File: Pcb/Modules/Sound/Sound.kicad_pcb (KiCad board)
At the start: 2 copper layers, 50.8 x 20.3 mm, 18 parts, among them J1 JACK_RJ45, U1 MAX4466, X1 HOLE, X2 HOLE, X3 HOLE, X4 HOLE

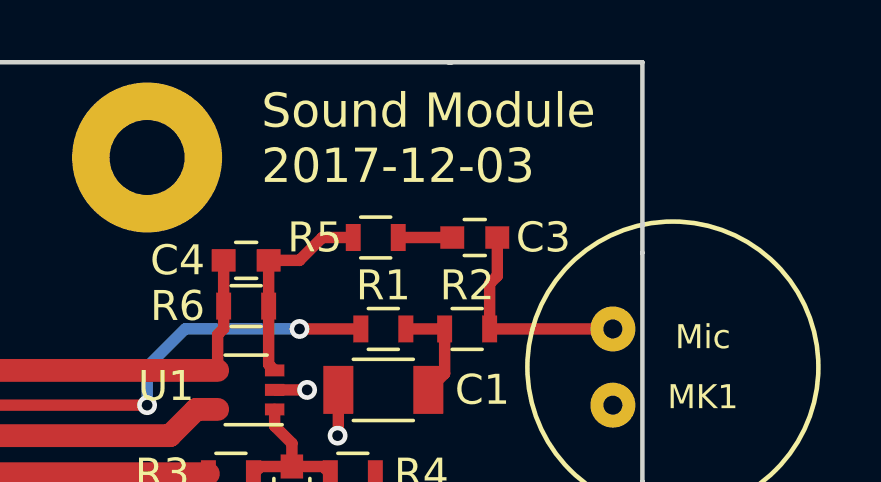
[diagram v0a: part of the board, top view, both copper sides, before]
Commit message: Update CA6 PCB.  Also update versions of all the module pcbs to match.
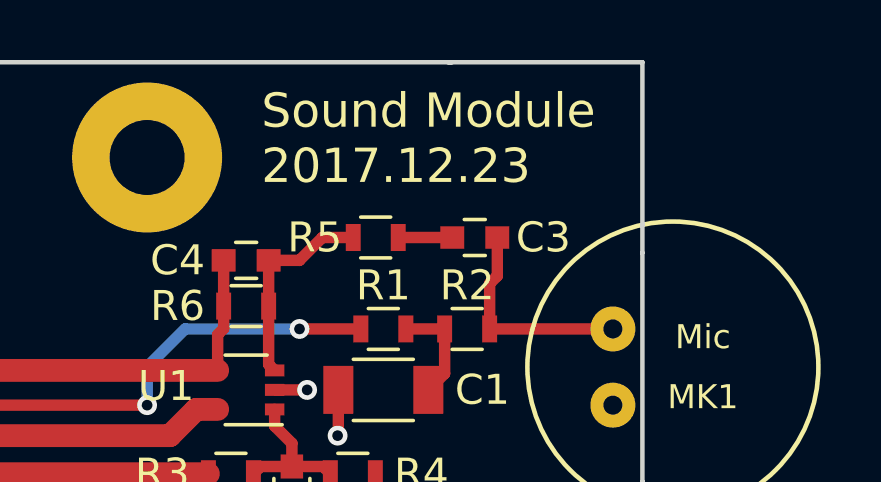
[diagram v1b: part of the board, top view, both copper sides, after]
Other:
- board text added: "Sound Module 2017.12.23"
- board text removed: "Sound Module 2017-12-03"
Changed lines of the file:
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@@
     (links 26)
     (no_connects 0)
-    (area 25.324999 25.324999 76.275001 45.795001)
+    (area 22.381869 24.0968 82.345401 47.1232)
     (thickness 1.6)
     (drawings 13)
@@
   (gr_line (start 69.85 45.72) (end 31.75 45.72) (angle 90) (layer Edge.Cuts) (width 0.15))
   (gr_line (start 31.75 25.4) (end 69.85 25.4) (angle 90) (layer Edge.Cuts) (width 0.15))
-  (gr_text "Sound Module\n2017-12-03" (at 63.5 27.94) (layer F.SilkS)
+  (gr_text "Sound Module\n2017.12.23" (at 63.5 27.94) (layer F.SilkS)
     (effects (font (size 1.143 1.143) (thickness 0.2286)) (justify left))
   )

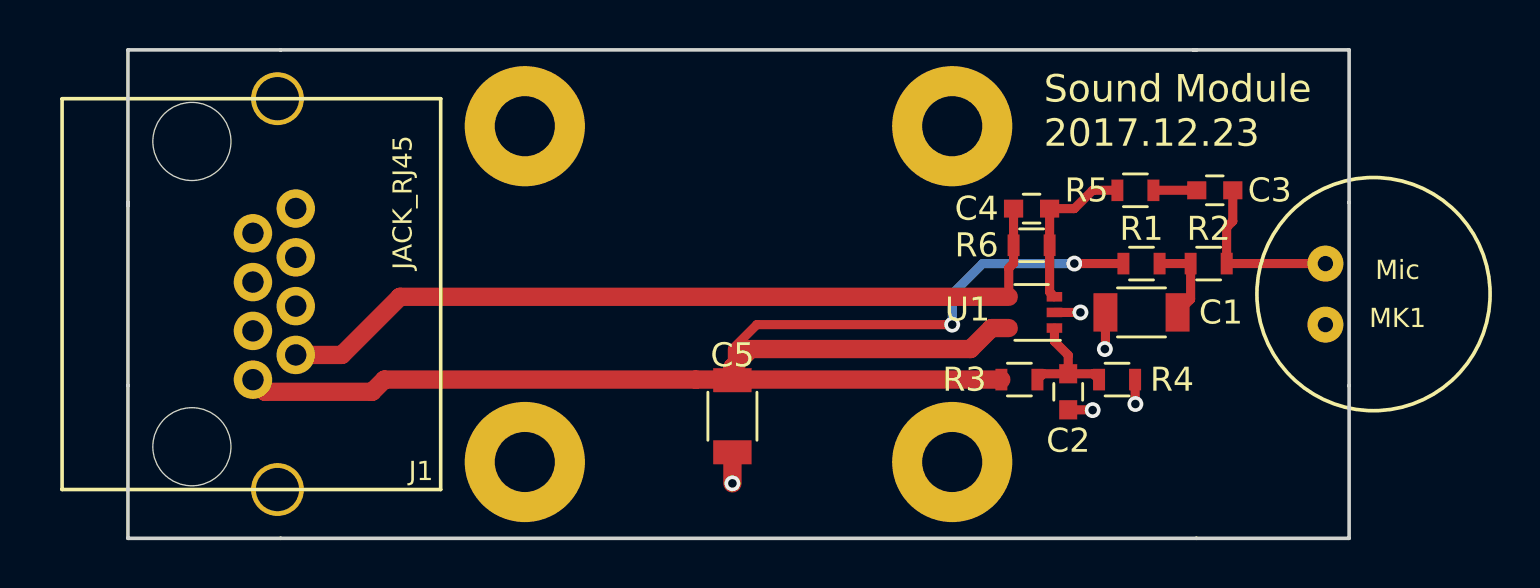
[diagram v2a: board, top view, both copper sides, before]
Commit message: Update module pcbs
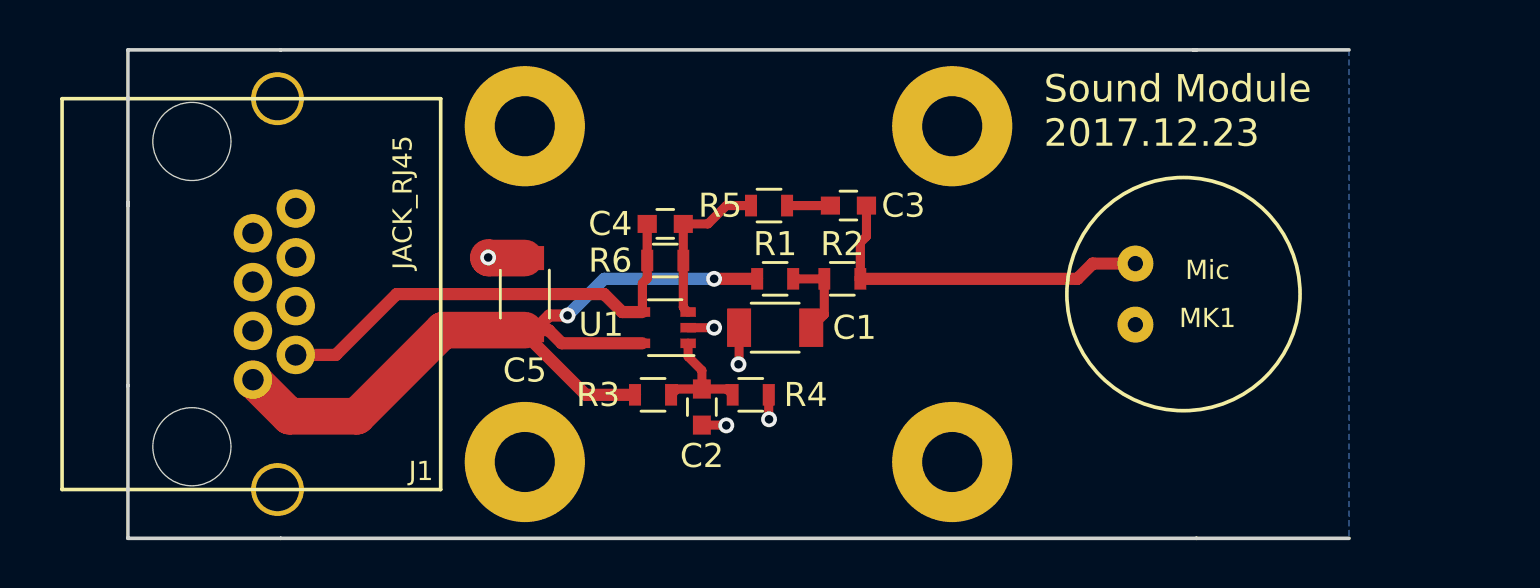
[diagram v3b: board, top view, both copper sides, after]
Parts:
- moved C2 15.3 mm to (49.3, 40.3)
- moved R2 15.3 mm to (55.1, 34.9)
- moved R3 15.3 mm to (47.2, 39.8)
- moved R4 15.3 mm to (51.3, 39.8)
- moved R5 15.3 mm to (52.1, 31.9)
- moved C1 15.3 mm to (52.3, 37.0)
- moved C3 15.3 mm to (55.4, 31.9)
- moved C4 15.3 mm to (47.8, 32.6)
- moved R1 15.3 mm to (52.3, 34.9)
- moved R6 15.3 mm to (47.8, 34.2)
- moved U1 15.3 mm to (47.8, 37.0)
- moved C5 10.0 mm to (41.9, 35.6), turned to 270 degrees
- moved MK1 7.91 mm to (69.3, 35.6)
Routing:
- net +3V3: track 65.6 -> 34.9 mm
- net /AN_VAL: track 34.4 -> 19.5 mm
- net Net-(C3-Pad1): track 7.01 -> 14.9 mm
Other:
- outline, holes or cut-outs redrawn

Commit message: Move holes on sound module to match other modules.  Updated silkscreens on other modules.  Generate gerbers
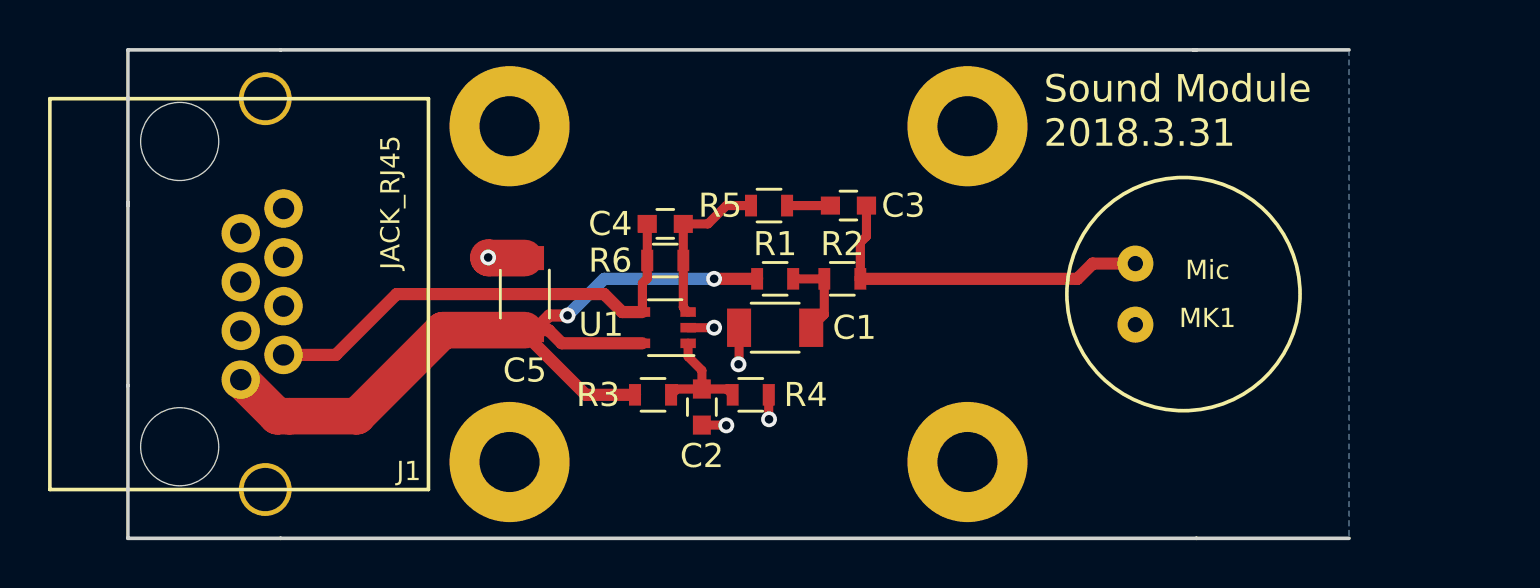
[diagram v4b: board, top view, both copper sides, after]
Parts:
- moved X3 0.64 mm to (60.3, 28.6)
- moved X4 0.64 mm to (60.3, 42.5)
- moved X1 0.63 mm to (41.3, 28.6)
- moved X2 0.63 mm to (41.3, 42.5)
- moved J1 0.51 mm to (30.0, 35.6)
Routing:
- net /AN_VAL: track 19.5 -> 20.0 mm
- net +3V3: track 34.9 -> 35.4 mm
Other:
- board text added: "Sound Module 2018.3.31"
- board text removed: "Sound Module 2017.12.23"
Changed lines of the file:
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@@
     (thickness 1.6)
     (drawings 11)
-    (tracks 65)
+    (tracks 66)
     (zones 0)
     (modules 18)
@@
   )
   (setup
-    (last_trace_width 0.254)
+    (last_trace_width 1.524)
     (user_trace_width 0.381)
     (user_trace_width 0.508)
@@
   )
   (module CA6:RJ45_pcbwing (layer F.Cu)
-    (at 30.48 35.56 270)
+    (at 29.972 35.56 270)
     (fp_text reference J1 (at 7.366 -7.112 360) (layer F.SilkS)
       (effects (font (size 0.8 0.8) (thickness 0.15)))
@@
   )
   (module Mounting_Holes:MountingHole_2.5mm_Pad (layer F.Cu)
-    (at 41.91 28.575)
+    (at 41.275 28.575)
     (descr "Mounting Hole 2.5mm")
     (tags "mounting hole 2.5mm")
@@
       (effects (font (size 1 1) (thickness 0.15)))
     )
-    (fp_text user %R (at 0.3 0) (layer F.Fab)
+    (fp_text user %R (at 0.3 0) (layer F.Fab) hide
       (effects (font (size 1 1) (thickness 0.15)))
     )
@@
   )
   (module Mounting_Holes:MountingHole_2.5mm_Pad (layer F.Cu)
-    (at 41.91 42.545)
+    (at 41.275 42.545)
     (descr "Mounting Hole 2.5mm")
     (tags "mounting hole 2.5mm")
@@
       (effects (font (size 1 1) (thickness 0.15)))
     )
-    (fp_text user %R (at 0.3 0) (layer F.Fab)
+    (fp_text user %R (at 0.3 0) (layer F.Fab) hide
       (effects (font (size 1 1) (thickness 0.15)))
     )
@@
   )
   (module Mounting_Holes:MountingHole_2.5mm_Pad (layer F.Cu)
-    (at 59.69 28.575)
+    (at 60.325 28.575)
     (descr "Mounting Hole 2.5mm")
     (tags "mounting hole 2.5mm")
@@
       (effects (font (size 1 1) (thickness 0.15)))
     )
-    (fp_text user %R (at 0.3 0) (layer F.Fab)
+    (fp_text user %R (at 0.3 0) (layer F.Fab) hide
       (effects (font (size 1 1) (thickness 0.15)))
     )
@@
   )
   (module Mounting_Holes:MountingHole_2.5mm_Pad (layer F.Cu)
-    (at 59.69 42.545)
+    (at 60.325 42.545)
     (descr "Mounting Hole 2.5mm")
     (tags "mounting hole 2.5mm")
@@
       (effects (font (size 1 1) (thickness 0.15)))
     )
-    (fp_text user %R (at 0.3 0) (layer F.Fab)
+    (fp_text user %R (at 0.3 0) (layer F.Fab) hide
       (effects (font (size 1 1) (thickness 0.15)))
     )
@@
   (gr_line (start 69.85 45.72) (end 31.75 45.72) (angle 90) (layer Edge.Cuts) (width 0.15))
   (gr_line (start 31.75 25.4) (end 69.85 25.4) (angle 90) (layer Edge.Cuts) (width 0.15))
-  (gr_text "Sound Module\n2017.12.23" (at 63.5 27.94) (layer F.SilkS)
+  (gr_text "Sound Module\n2018.3.31" (at 63.5 27.94) (layer F.SilkS)
     (effects (font (size 1.143 1.143) (thickness 0.2286)) (justify left))
   )
@@
   (segment (start 50.316 39.509) (end 50.558 39.751) (width 0.381) (layer F.Cu) (net 3))
   (segment (start 54.622 31.877) (end 52.82 31.877) (width 0.381) (layer F.Cu) (net 4))
-  (segment (start 32.38 38.09) (end 34.046 38.09) (width 0.508) (layer F.Cu) (net 5))
+  (segment (start 31.872 38.09) (end 34.046 38.09) (width 0.508) (layer F.Cu) (net 5))
+  (segment (start 34.046 38.09) (end 36.576 35.56) (width 0.508) (layer F.Cu) (net 5))
+  (segment (start 36.576 35.56) (end 45.212 35.56) (width 0.508) (layer F.Cu) (net 5))
+  (segment (start 45.212 35.56) (end 45.959 36.307) (width 0.508) (layer F.Cu) (net 5))
   (segment (start 45.959 36.307) (end 46.802 36.307) (width 0.508) (layer F.Cu) (net 5))
-  (segment (start 45.212 35.56) (end 45.959 36.307) (width 0.508) (layer F.Cu) (net 5))
-  (segment (start 36.576 35.56) (end 45.212 35.56) (width 0.508) (layer F.Cu) (net 5))
-  (segment (start 34.046 38.09) (end 36.576 35.56) (width 0.508) (layer F.Cu) (net 5))
   (segment (start 46.802 36.307) (end 46.802 35.113) (width 0.381) (layer F.Cu) (net 5))
   (segment (start 47.002 34.913) (end 47.002 34.163) (width 0.381) (layer F.Cu) (net 5))
@@
   (segment (start 49.53 32.639) (end 48.502 32.639) (width 0.381) (layer F.Cu) (net 6))
   (segment (start 50.292 31.877) (end 49.53 32.639) (width 0.381) (layer F.Cu) (net 6))
+  (segment (start 32.12 40.64) (end 31.612 40.64) (width 1.524) (layer F.Cu) (net 7))
+  (segment (start 32.12 40.64) (end 34.925 40.64) (width 1.524) (layer F.Cu) (net 7))
+  (segment (start 41.91 37.06) (end 38.505 37.06) (width 1.524) (layer F.Cu) (net 7))
+  (segment (start 34.925 40.64) (end 38.505 37.06) (width 1.524) (layer F.Cu) (net 7))
+  (segment (start 31.612 40.64) (end 30.092 39.12) (width 1.524) (layer F.Cu) (net 7))
   (segment (start 41.91 37.06) (end 42.315 37.06) (width 0.508) (layer F.Cu) (net 7))
   (segment (start 42.315 37.06) (end 42.926 36.449) (width 0.508) (layer F.Cu) (net 7))
@@
   (segment (start 41.91 37.211) (end 44.45 39.751) (width 0.508) (layer F.Cu) (net 7))
   (segment (start 44.45 39.751) (end 46.494 39.751) (width 0.508) (layer F.Cu) (net 7))
-  (segment (start 34.925 40.64) (end 38.505 37.06) (width 1.524) (layer F.Cu) (net 7))
-  (segment (start 38.505 37.06) (end 41.91 37.06) (width 1.524) (layer F.Cu) (net 7))
-  (segment (start 32.12 40.64) (end 34.925 40.64) (width 1.524) (layer F.Cu) (net 7))
-  (segment (start 30.6 39.12) (end 32.12 40.64) (width 1.524) (layer F.Cu) (net 7))
   (segment (start 55.868 34.925) (end 64.897 34.925) (width 0.508) (layer F.Cu) (net 8))
   (segment (start 65.532 34.29) (end 67.31 34.29) (width 0.508) (layer F.Cu) (net 8))

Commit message: Update pcbs
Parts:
- moved MK1 1.68 mm to (71.0, 35.6)
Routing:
- net Net-(C3-Pad1): track 14.9 -> 16.5 mm
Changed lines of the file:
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@@
     (links 26)
     (no_connects 0)
-    (area 22.381869 24.0968 76.300001 47.1232)
+    (area 21.873869 24.0968 76.300001 47.1232)
     (thickness 1.6)
     (drawings 11)
@@
   )
   (setup
-    (last_trace_width 1.524)
+    (last_trace_width 0.254)
     (user_trace_width 0.381)
     (user_trace_width 0.508)
@@
   )
   (module CA6:MIC_CMA-4544PF (layer F.Cu)
-    (at 69.31 35.56 180)
+    (at 70.993 35.56 180)
     (tags "CMS SM")
     (attr smd)
@@
   (segment (start 44.45 39.751) (end 46.494 39.751) (width 0.508) (layer F.Cu) (net 7))
   (segment (start 55.868 34.925) (end 64.897 34.925) (width 0.508) (layer F.Cu) (net 8))
-  (segment (start 65.532 34.29) (end 67.31 34.29) (width 0.508) (layer F.Cu) (net 8))
+  (segment (start 65.532 34.29) (end 68.993 34.29) (width 0.508) (layer F.Cu) (net 8) (status 20))
   (segment (start 64.897 34.925) (end 65.532 34.29) (width 0.508) (layer F.Cu) (net 8))
   (segment (start 55.868 34.925) (end 55.868 33.413) (width 0.381) (layer F.Cu) (net 8))

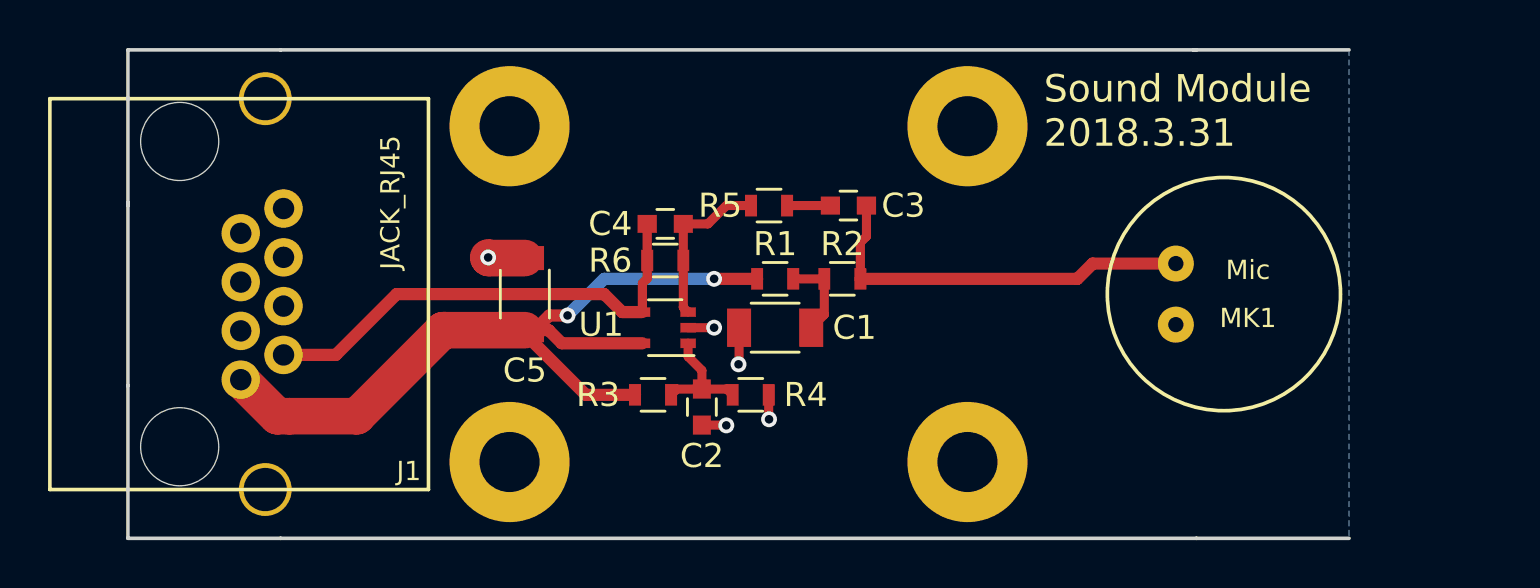
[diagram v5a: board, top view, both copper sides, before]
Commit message: Update module pcbs to fix minor issues and round corners
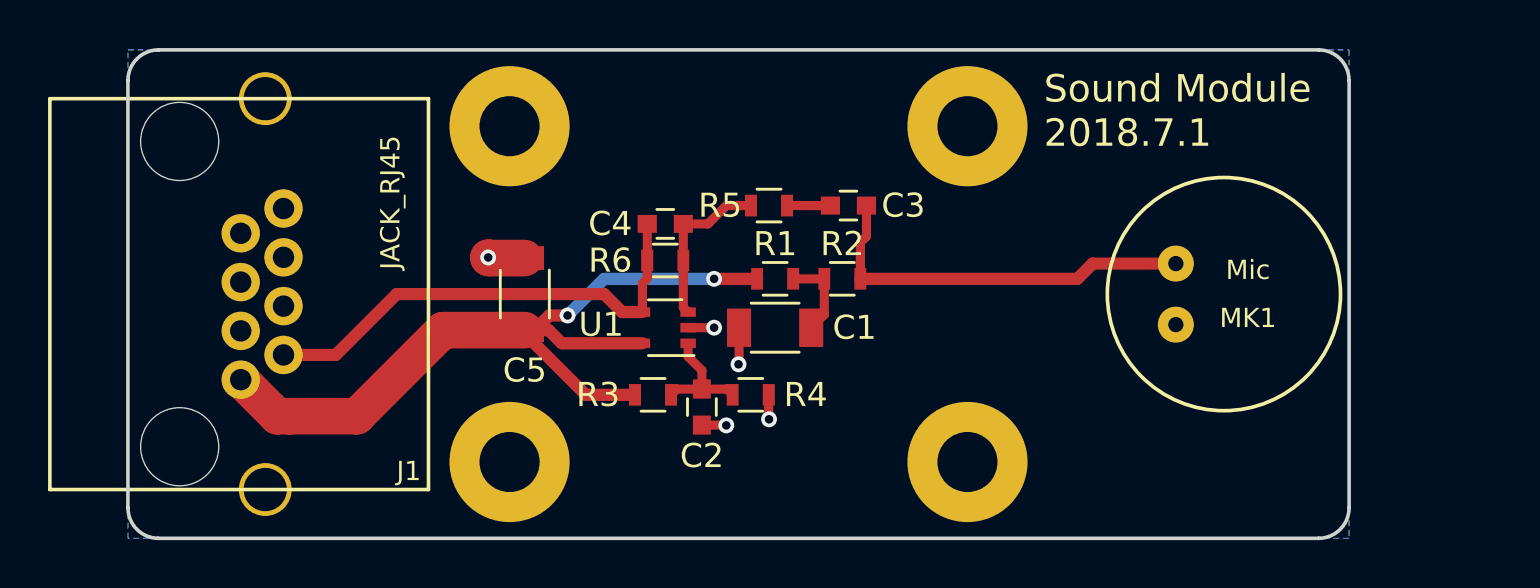
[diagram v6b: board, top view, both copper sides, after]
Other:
- outline, holes or cut-outs redrawn
- board text added: "Sound Module 2018.7.1"
- board text removed: "Sound Module 2018.3.31"
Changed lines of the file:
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@@
     (area 21.873869 24.0968 76.300001 47.1232)
     (thickness 1.6)
-    (drawings 11)
+    (drawings 9)
     (tracks 66)
     (zones 0)
@@
     )
   )
-  (gr_line (start 76.2 25.4) (end 76.2 45.72) (layer Eco2.User) (width 0.2))
-  (gr_line (start 25.4 45.72) (end 31.75 45.72) (angle 90) (layer Edge.Cuts) (width 0.15))
-  (gr_line (start 25.4 39.37) (end 25.4 45.72) (angle 90) (layer Edge.Cuts) (width 0.15))
-  (gr_line (start 25.4 25.4) (end 25.4 31.877) (angle 90) (layer Edge.Cuts) (width 0.15))
-  (gr_line (start 31.75 25.4) (end 25.4 25.4) (angle 90) (layer Edge.Cuts) (width 0.15))
-  (gr_line (start 76.2 45.72) (end 69.85 45.72) (angle 90) (layer Edge.Cuts) (width 0.15))
-  (gr_line (start 76.2 25.4) (end 69.723 25.4) (angle 90) (layer Edge.Cuts) (width 0.15))
-  (gr_line (start 25.4 31.75) (end 25.4 39.37) (angle 90) (layer Edge.Cuts) (width 0.15))
-  (gr_line (start 69.85 45.72) (end 31.75 45.72) (angle 90) (layer Edge.Cuts) (width 0.15))
-  (gr_line (start 31.75 25.4) (end 69.85 25.4) (angle 90) (layer Edge.Cuts) (width 0.15))
-  (gr_text "Sound Module\n2018.3.31" (at 63.5 27.94) (layer F.SilkS)
+  (gr_line (start 25.4 44.45) (end 25.4 26.67) (angle 90) (layer Edge.Cuts) (width 0.15))
+  (gr_line (start 74.93 45.72) (end 26.67 45.72) (angle 90) (layer Edge.Cuts) (width 0.15))
+  (gr_line (start 76.2 26.67) (end 76.2 44.45) (angle 90) (layer Edge.Cuts) (width 0.15))
+  (gr_line (start 26.67 25.4) (end 74.93 25.4) (angle 90) (layer Edge.Cuts) (width 0.15))
+  (gr_arc (start 74.93 26.67) (end 74.93 25.4) (angle 90) (layer Edge.Cuts) (width 0.15))
+  (gr_arc (start 74.93 44.45) (end 76.2 44.45) (angle 90) (layer Edge.Cuts) (width 0.15))
+  (gr_arc (start 26.67 44.45) (end 26.67 45.72) (angle 90) (layer Edge.Cuts) (width 0.15))
+  (gr_arc (start 26.67 26.67) (end 25.4 26.67) (angle 90) (layer Edge.Cuts) (width 0.15))
+  (gr_text "Sound Module\n2018.7.1" (at 63.5 27.94) (layer F.SilkS)
     (effects (font (size 1.143 1.143) (thickness 0.2286)) (justify left))
   )
